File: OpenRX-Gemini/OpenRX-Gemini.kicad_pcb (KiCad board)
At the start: 6 copper layers, 54 x 14.2 mm, 194 parts, among them T1 0900PC16J0042001E, T4 0900PC16J0042001E, T5 0900PC16J0042001E, U1 ESP32-C3FH4, U1 OW7EL89CENUYO3YLC-32M, U15 RFX2401C, U16 SKY13414-485LF, U17 RFX2401C, U18 SKY13414-485LF, U2 LR1121IMLTRT, U2 TLV75533PDQNR, U3 ESP32-C3FH4, U3 SX1281IMLTRT, U3 TS2306A 240GF MSM 9_C2976675, U4 LR1121IMLTRT, U4 TS2306A 240GF MSM 9_C2976675, U5 OW7EL89CENUYO3YLC-32M, U6 TLV75533PDQNR, U7 RFX2401C, U8 SKY13414-485LF, U9 LR1121IMLTRT, X1 CJ17-400001010B20

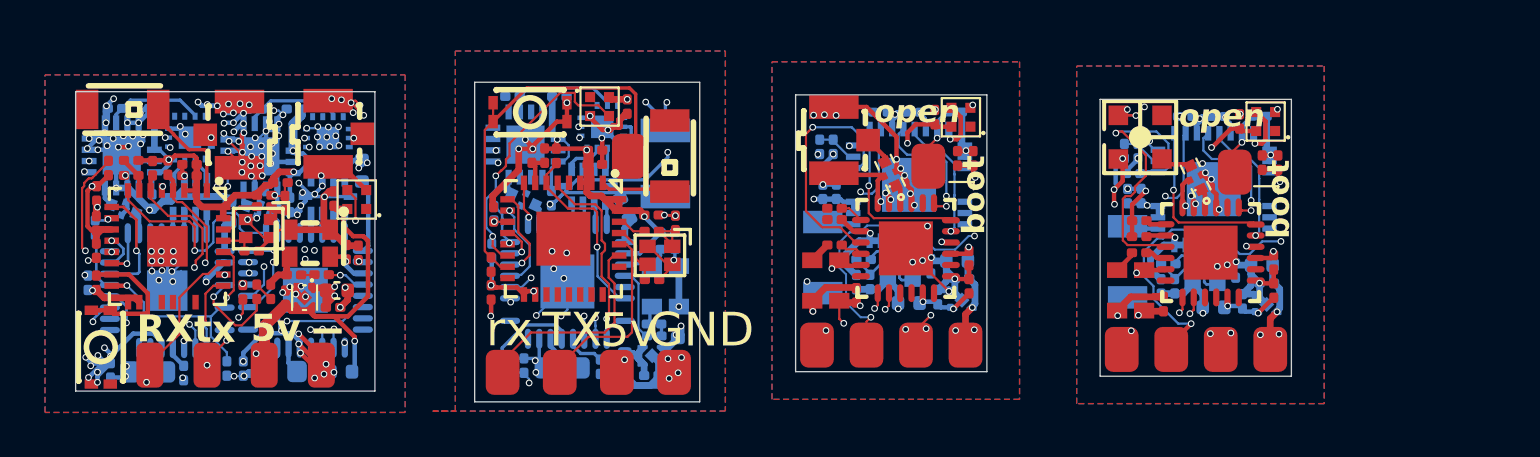
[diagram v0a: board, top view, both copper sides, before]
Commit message: switch to 0.2mm vias
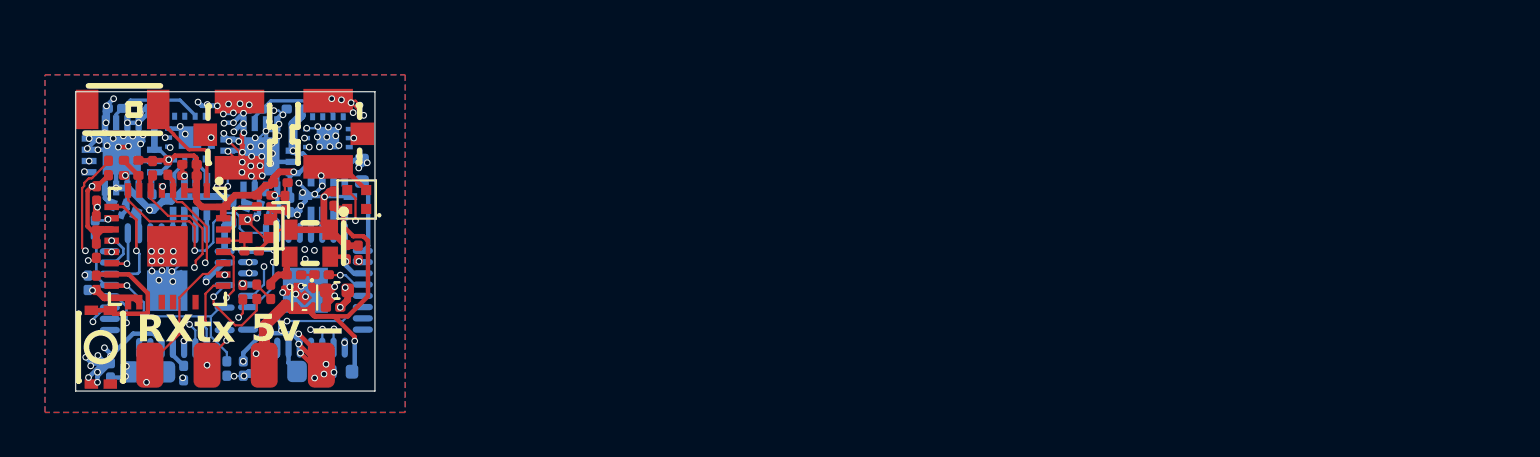
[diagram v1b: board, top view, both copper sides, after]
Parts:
- removed the AE1 at (87.8, 47.6)
- removed the AE1 at (108.1, 52.3)
- removed the AE1 at (94.6, 52.1)
- removed AE2: 47948-0001, OpenRX-Shared:ANT-SMD_47948-0001
- removed the C1 at (84.4, 47.4)
- removed the C1 at (96.7, 53.2)
- removed the C1 at (110.2, 53.4)
- removed the C10 at (100.7, 53.1)
- removed the C10 at (114.3, 53.3)
- removed the C11 at (100.5, 47.7)
- removed the C11 at (114.1, 47.9)
- removed the C11 at (88.1, 56.2)
- removed the C12 at (110.7, 45.9)
- removed the C12 at (85.8, 56.9)
- removed the C12 at (97.1, 45.7)
- removed the C13 at (96.0, 53.8)
- removed the C13 at (109.7, 54.2)
- removed the C13 at (87.1, 55.6)
- removed the C14 at (108.6, 51.2)
- removed the C14 at (95.1, 50.4)
- removed the C14 at (82.5, 49.5)
- removed the C15 at (99.7, 53.9)
- removed the C15 at (113.2, 54.1)
- removed the C15 at (82.9, 45.0)
- removed the C16 at (80.8, 45.0)
- removed the C16 at (111.9, 54.3)
- removed the C16 at (98.4, 54.1)
- removed the C17 at (114.6, 52.3)
- removed the C17 at (101.1, 52.1)
- removed the C18 at (85.9, 45.4)
- removed the C18 at (101.1, 53.4)
- removed the C18 at (114.6, 53.6)
- removed C19: 1uF, Capacitor_SMD:C_0201_0603Metric
- removed C19 (x2): 1nF, Capacitor_SMD:C_0201_0603Metric
- removed the C2 at (84.4, 48.0)
- removed the C2 at (94.4, 47.2)
- removed the C2 at (108.0, 47.4)
- removed the C20 at (108.6, 50.5)
- removed the C20 at (95.1, 49.9)
- removed the C20 at (85.8, 49.9)
- removed C21, C23, C5 (x3): 100nF, Capacitor_SMD:C_0201_0603Metric
- removed the C22 at (84.7, 57.0)
- removed the C24 at (81.3, 56.9)
- removed the C3 at (79.8, 53.7)
- removed the C3 at (99.4, 52.5)
- removed the C3 at (112.9, 52.7)
- removed the C4 at (109.6, 53.4)
- removed the C4 at (96.0, 53.2)
- removed the C4 at (80.7, 56.9)
- removed the C6 at (88.0, 50.6)
- removed the C6 at (108.1, 49.4)
- removed the C6 at (94.6, 49.2)
- removed the C7 at (113.1, 46.1)
- removed the C7 at (87.0, 53.1)
- removed the C7 at (99.5, 45.9)
- removed the C8 at (81.6, 47.6)
- removed the C8 at (100.5, 52.3)
- removed the C8 at (114.1, 52.5)
- removed the C9 at (101.2, 47.7)
- removed the C9 at (114.8, 47.9)
- removed the C9 at (86.9, 57.4)
- removed the D1 at (114.2, 46.1)
- removed the D1 at (100.7, 45.9)
- removed the D1 at (84.6, 45.4)
- removed FL1 (x3): 2450FM07D0034T, OpenRX-Shared:FILTER-SMD_4P-L1.0-W0.5-L
- removed JP1 (x2): U.FL-R-SMT-1(80), OpenRX-Shared:RF-SMD_FRF05002-JSS103M
- removed the L1 at (83.0, 57.0)
- removed the L1 at (109.9, 52.4)
- removed the L1 at (96.4, 52.2)
- removed the L2 at (87.0, 51.0)
- removed OSC1 (x2): OW7EL89CENUNFAYLC-52M, OpenRX-Shared:OSC-SMD_4P-L2.0-W1.6-BL_TXC_7Z
- removed the R1 at (82.2, 47.6)
- removed the R1 at (95.0, 47.2)
- removed the R1 at (108.6, 47.4)
- removed the R2 at (108.3, 48.4)
- removed the R2 at (94.8, 48.2)
- removed the R2 at (80.0, 50.1)
- removed the R3 at (79.8, 52.4)
- removed the R3 at (98.6, 45.7)
- removed the R3 at (112.1, 45.9)
- removed the R4 at (82.7, 47.6)
- removed the R4 at (100.4, 45.6)
- removed the R4 at (114.0, 45.8)
- removed the R5 at (79.8, 51.8)
- removed the R6 at (87.1, 55.1)
- removed T1: 0900PC16J0042001E, OpenRX-Shared:FILTER-SMD_10P-L2.0-W1.6-BL
- removed the TP1 at (107.8, 56.2)
- removed the TP1 at (80.3, 57.2)
- removed the TP1 at (94.3, 56.0)
- removed the TP2 at (82.9, 57.2)
- removed the TP2 at (96.5, 56.0)
- removed the TP2 at (110.0, 56.2)
- removed the TP3 at (100.9, 56.0)
- removed the TP3 at (85.4, 57.2)
- removed the TP3 at (114.4, 56.2)
- removed the TP4 at (98.7, 56.0)
- removed the TP4 at (88.0, 57.2)
- removed the TP4 at (112.2, 56.2)
- removed TP5: Boot, OpenRX-Shared:SolderPad_1.2x2.0mm
- removed TP5 (x2): GND, OpenRX-Shared:SolderPad_1.2x2.0mm
- removed the U1 at (83.0, 51.3)
- removed the U1 at (111.9, 49.1)
- removed the U1 at (98.4, 48.9)
- removed the U2 at (114.3, 54.2)
- removed the U2 at (87.0, 56.5)
- removed the U2 at (100.7, 54.0)
- removed the U3 at (111.8, 51.9)
- removed the U3 at (98.2, 51.7)
- removed the U3 at (81.5, 45.7)
- removed the U4 at (83.2, 53.2)
- removed U5: OW7EL89CENUYO3YLC-32M, OpenRX-Shared:OSC-SMD_4P-L2.0-W1.6-BL_TXC_7Z
- removed U7: RFX2401C, OpenRX-Shared:QFN-16_L3.0-W3.0-P0.50-BL-EP1.7
- removed U8: SKY13414-485LF, OpenRX-Shared:QFN-14_L2.0-W2.0-P0.45-BL-EP
- removed the X1 at (87.3, 52.0)
- removed the X1 at (98.0, 52.7)
- removed the X1 at (111.5, 52.9)
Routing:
- net GND: track 296.8 -> 155.9 mm, vias 220 -> 136
- net +3V3: track 121.9 -> 50.4 mm, vias 42 -> 14
- net +5V: track 66.8 -> 17.7 mm, vias 12 -> 2
- net Net-(U1-U0RXD): track 32.2 -> 0.00 mm, vias 4 -> 0
- net Net-(U1-U0TXD): track 27.9 -> 0.00 mm, vias 2 -> 0
- net /ESP32-C3 + LR1121 Mono/BUTTON: track 18.2 -> 0.00 mm
- net /ESP32-C3 + SX1281 Core/RST: track 13.2 -> 0.00 mm, vias 1 -> 0
- net /ESP32-C3 + LR1121 Mono/LED: track 12.0 -> 0.00 mm, vias 2 -> 0
- net /ESP32-C3 + SX1281 Core (UFL)/RST: track 11.8 -> 0.00 mm, vias 1 -> 0
- net /ESP32-C3 + LR1121 Mono/DIO8-1: track 10.2 -> 0.00 mm, vias 2 -> 0
- net /ESP32-C3 + SX1281 Core/DIO1: track 10.0 -> 0.00 mm, vias 2 -> 0
- net /ESP32-C3 + SX1281 Core (UFL)/DIO1: track 10.0 -> 0.00 mm, vias 2 -> 0
- net /ESP32-C3 + SX1281 Core/BUSY: track 9.55 -> 0.00 mm, vias 2 -> 0
- net /ESP32-C3 + LR1121 Mono/DIO7-1: track 9.16 -> 0.00 mm, vias 2 -> 0
- net /ESP32-C3 + SX1281 Core (UFL)/BUSY: track 8.60 -> 0.00 mm, vias 2 -> 0
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- removed copper zone on In3.Cu, net +3V3
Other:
- board size 54 x 14.2 mm -> 13.3 x 13.3 mm
- board text removed: "GND"
- board text removed: "TX"
- board text removed: "boot"
- board text removed: "open"
- board text removed: "rx"

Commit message: Update OpenRX-Gemini.kicad_pcb
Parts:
- added AE1: 2450AT18A100E, OpenRX-Shared:ANT-SMD_L3.2-W1.6, F.Cu at (94.9, 47.0)
- added AE1: 2450AT18A100E, OpenRX-Shared:ANT-SMD_L3.2-W1.6, B.Cu at (115.6, 51.6)
- added AE1: 2450AT18A100E, OpenRX-Shared:ANT-SMD_L3.2-W1.6, B.Cu at (102.0, 51.6)
- added AE2: 47948-0001, OpenRX-Shared:ANT-SMD_47948-0001, F.Cu at (116.2, 46.1)
- added C1: 100nF, Capacitor_SMD:C_0201_0603Metric, F.Cu at (91.5, 46.7)
- added C1: 18pF, Capacitor_SMD:C_0201_0603Metric, B.Cu at (104.1, 52.7)
- added C1: 18pF, Capacitor_SMD:C_0201_0603Metric, B.Cu at (117.7, 52.7)
- added C10: 1uF, Capacitor_SMD:C_0201_0603Metric, B.Cu at (108.2, 52.6)
- added C10: 1uF, Capacitor_SMD:C_0201_0603Metric, B.Cu at (121.8, 52.6)
- added C11: 100nF, Capacitor_SMD:C_0201_0603Metric, F.Cu at (108.0, 47.2)
- added C11: 100nF, Capacitor_SMD:C_0201_0603Metric, F.Cu at (121.6, 47.2)
- added C11: 10uF, Capacitor_SMD:C_0402_1005Metric, B.Cu at (95.2, 55.5)
- added C12: 100nF, Capacitor_SMD:C_0201_0603Metric, B.Cu at (104.6, 45.1)
- added C12: 100nF, Capacitor_SMD:C_0201_0603Metric, B.Cu at (118.2, 45.1)
- added C12: 10uF, Capacitor_SMD:C_0402_1005Metric, B.Cu at (92.9, 56.2)
- added C13: 100nF, Capacitor_SMD:C_0201_0603Metric, F.Cu at (103.5, 53.3)
- added C13: 100nF, Capacitor_SMD:C_0201_0603Metric, F.Cu at (117.2, 53.5)
- added C13: 10pF, Capacitor_SMD:C_0201_0603Metric, B.Cu at (94.2, 55.0)
- added C14: 100nF, Capacitor_SMD:C_0201_0603Metric, F.Cu at (116.1, 50.5)
- added C14: 100nF, Capacitor_SMD:C_0201_0603Metric, F.Cu at (102.5, 49.9)
- added C14: 1uF, Capacitor_SMD:C_0201_0603Metric, B.Cu at (89.6, 48.8)
- added C15: 220pF, Capacitor_SMD:C_0201_0603Metric, B.Cu at (90.0, 44.3)
- added C15: 1uF, Capacitor_SMD:C_0201_0603Metric, B.Cu at (120.7, 53.4)
- added C15: 1uF, Capacitor_SMD:C_0201_0603Metric, B.Cu at (107.1, 53.4)
- added C16: 0.3pF, Capacitor_SMD:C_0201_0603Metric, B.Cu at (87.9, 44.3)
- added C16: 10uF, Capacitor_SMD:C_0402_1005Metric, B.Cu at (105.8, 53.6)
- added C16: 10uF, Capacitor_SMD:C_0402_1005Metric, B.Cu at (119.4, 53.6)
- added C17: 100nF, Capacitor_SMD:C_0201_0603Metric, F.Cu at (122.1, 51.6)
- added C17: 100nF, Capacitor_SMD:C_0201_0603Metric, F.Cu at (108.5, 51.6)
- added C18: 100nF, Capacitor_SMD:C_0201_0603Metric, F.Cu at (122.1, 52.9)
- added C18: 100nF, Capacitor_SMD:C_0201_0603Metric, F.Cu at (93.0, 44.8)
- added C18: 100nF, Capacitor_SMD:C_0201_0603Metric, F.Cu at (108.5, 52.9)
- added C19: 1uF, Capacitor_SMD:C_0201_0603Metric, F.Cu at (94.1, 49.6)
- added C19: 1nF, Capacitor_SMD:C_0201_0603Metric, F.Cu at (102.5, 51.0)
- added C19: 1nF, Capacitor_SMD:C_0201_0603Metric, F.Cu at (116.1, 51.2)
- added C2: 100nF, Capacitor_SMD:C_0201_0603Metric, F.Cu at (91.5, 47.3)
- added C2: 1uF, Capacitor_SMD:C_0201_0603Metric, B.Cu at (115.5, 46.7)
- added C2: 1uF, Capacitor_SMD:C_0201_0603Metric, B.Cu at (101.9, 46.7)
- added C20: 470nF, Capacitor_SMD:C_0201_0603Metric, F.Cu at (116.1, 49.8)
- added C20: 470nF, Capacitor_SMD:C_0201_0603Metric, F.Cu at (102.5, 49.4)
- added C20: 4.7uF, Capacitor_SMD:C_0402_1005Metric, B.Cu at (92.9, 49.3)
- added C21: 100nF, Capacitor_SMD:C_0201_0603Metric, B.Cu at (94.8, 50.4)
- added C22: 100nF, Capacitor_SMD:C_0201_0603Metric, B.Cu at (91.8, 56.3)
- added C23: 100nF, Capacitor_SMD:C_0201_0603Metric, B.Cu at (94.8, 51.1)
- added C24: 100nF, Capacitor_SMD:C_0201_0603Metric, B.Cu at (88.4, 56.3)
- added C3: 100nF, Capacitor_SMD:C_0201_0603Metric, F.Cu at (86.9, 53.0)
- added C3: 18pF, Capacitor_SMD:C_0201_0603Metric, B.Cu at (106.8, 52.0)
- added C3: 18pF, Capacitor_SMD:C_0201_0603Metric, B.Cu at (120.4, 52.0)
- added C4: 100nF, Capacitor_SMD:C_0201_0603Metric, B.Cu at (87.8, 56.3)
- added C4: 1uF, Capacitor_SMD:C_0201_0603Metric, B.Cu at (117.1, 52.7)
- added C4: 1uF, Capacitor_SMD:C_0201_0603Metric, B.Cu at (103.5, 52.7)
- added C5: 100nF, Capacitor_SMD:C_0201_0603Metric, F.Cu at (87.0, 49.6)
- added C5: 100nF, Capacitor_SMD:C_0201_0603Metric, B.Cu at (116.2, 48.7)
- added C5: 100nF, Capacitor_SMD:C_0201_0603Metric, B.Cu at (102.6, 48.7)
- added C6: 18pF, Capacitor_SMD:C_0201_0603Metric, F.Cu at (95.1, 49.9)
- added C6: 100nF, Capacitor_SMD:C_0201_0603Metric, B.Cu at (115.6, 48.7)
- added C6: 100nF, Capacitor_SMD:C_0201_0603Metric, B.Cu at (102.0, 48.7)
- added C7: 100nF, Capacitor_SMD:C_0201_0603Metric, F.Cu at (107.0, 45.4)
- added C7: 100nF, Capacitor_SMD:C_0201_0603Metric, F.Cu at (120.6, 45.4)
- added C7: 18pF, Capacitor_SMD:C_0201_0603Metric, F.Cu at (94.1, 52.5)
- added C8: 1uF, Capacitor_SMD:C_0201_0603Metric, F.Cu at (88.7, 47.0)
- added C8: 10uF, Capacitor_SMD:C_0402_1005Metric, B.Cu at (121.6, 51.8)
- added C8: 10uF, Capacitor_SMD:C_0402_1005Metric, B.Cu at (108.0, 51.8)
- added C9: 100nF, Capacitor_SMD:C_0201_0603Metric, F.Cu at (108.7, 47.2)
- added C9: 100nF, Capacitor_SMD:C_0201_0603Metric, F.Cu at (122.3, 47.2)
- added C9: 1uF, Capacitor_SMD:C_0201_0603Metric, B.Cu at (94.0, 56.7)
- added D1: XL-1010RGBC-WS2812B, OpenRX-Shared:LED-SMD_4P-L1.0-W1.0-TL_XL-1010RGBC-WS2812B, F.Cu at (108.2, 45.4)
- added D1: XL-1010RGBC-WS2812B, OpenRX-Shared:LED-SMD_4P-L1.0-W1.0-TL_XL-1010RGBC-WS2812B, F.Cu at (91.8, 44.8)
- added D1: XL-1010RGBC-WS2812B, OpenRX-Shared:LED-SMD_4P-L1.0-W1.0-TL_XL-1010RGBC-WS2812B, F.Cu at (121.7, 45.4)
- added FL1: 2450FM07D0034T, OpenRX-Shared:FILTER-SMD_4P-L1.0-W0.5-L, F.Cu at (118.6, 47.9)
- added FL1: 2450FM07D0034T, OpenRX-Shared:FILTER-SMD_4P-L1.0-W0.5-L, F.Cu at (105.0, 47.9)
- added FL1: 2450FM07D0034T, OpenRX-Shared:FILTER-SMD_4P-L1.0-W0.5-L, B.Cu at (88.4, 48.9)
- added JP1: U.FL-R-SMT-1(80), OpenRX-Shared:RF-SMD_FRF05002-JSS103M, F.Cu at (103.3, 46.4)
- added JP1: U.FL-R-SMT-1(80), OpenRX-Shared:RF-SMD_FRF05002-JSS103M, B.Cu at (93.9, 47.3)
- added L1: 10uH, Inductor_SMD:L_0603_1608Metric, B.Cu at (90.1, 56.4)
- added L1: 24nH, Inductor_SMD:L_0201_0603Metric, B.Cu at (117.4, 51.7)
- added L1: 24nH, Inductor_SMD:L_0201_0603Metric, B.Cu at (103.8, 51.7)
- added L2: 24nH, Inductor_SMD:L_0201_0603Metric, F.Cu at (94.1, 50.3)
- added OSC1: OW7EL89CENUNFAYLC-52M, OpenRX-Shared:OSC-SMD_4P-L2.0-W1.6-BL_TXC_7Z, F.Cu at (102.2, 52.6)
- added OSC1: OW7EL89CENUNFAYLC-52M, OpenRX-Shared:OSC-SMD_4P-L2.0-W1.6-BL_TXC_7Z, F.Cu at (115.7, 52.9)
- added R1: 10k, Resistor_SMD:R_0201_0603Metric, F.Cu at (89.3, 47.0)
- added R1: 10k, Resistor_SMD:R_0201_0603Metric, B.Cu at (102.5, 46.7)
- added R1: 10k, Resistor_SMD:R_0201_0603Metric, B.Cu at (116.0, 46.7)
- added R2: 10k, Resistor_SMD:R_0201_0603Metric, B.Cu at (115.8, 47.7)
- added R2: 10k, Resistor_SMD:R_0201_0603Metric, B.Cu at (87.1, 49.5)
- added R2: 10k, Resistor_SMD:R_0201_0603Metric, B.Cu at (102.3, 47.7)
- added R3: 10k, Resistor_SMD:R_0201_0603Metric, F.Cu at (86.9, 51.8)
- added R3: 10k, Resistor_SMD:R_0201_0603Metric, B.Cu at (119.6, 45.1)
- added R3: 10k, Resistor_SMD:R_0201_0603Metric, B.Cu at (106.0, 45.1)
- added R4: 10k, Resistor_SMD:R_0201_0603Metric, F.Cu at (89.8, 47.0)
- added R4: 10k, Resistor_SMD:R_0201_0603Metric, B.Cu at (107.9, 45.1)
- added R4: 10k, Resistor_SMD:R_0201_0603Metric, B.Cu at (121.5, 45.1)
- added R5: 10k, Resistor_SMD:R_0201_0603Metric, B.Cu at (87.0, 51.2)
- added R6: 220R, Resistor_SMD:R_0201_0603Metric, B.Cu at (94.2, 54.4)
- added T1: 0900PC16J0042001E, OpenRX-Shared:FILTER-SMD_10P-L2.0-W1.6-BL, B.Cu at (91.3, 48.3)
- added TP1: RX, OpenRX-Shared:SolderPad_1.2x2.0mm, F.Cu at (115.3, 55.5)
- added TP1: RX, OpenRX-Shared:SolderPad_1.2x2.0mm, F.Cu at (101.8, 55.5)
- added TP1: RX, OpenRX-Shared:SolderPad_1.2x2.0mm, F.Cu at (87.4, 56.6)
- added TP2: TX, OpenRX-Shared:SolderPad_1.2x2.0mm, F.Cu at (104.0, 55.5)
- added TP2: TX, OpenRX-Shared:SolderPad_1.2x2.0mm, F.Cu at (117.5, 55.5)
- added TP2: TX, OpenRX-Shared:SolderPad_1.2x2.0mm, F.Cu at (90.0, 56.6)
- added TP3: 5V, OpenRX-Shared:SolderPad_1.2x2.0mm, F.Cu at (108.4, 55.5)
- added TP3: 5V, OpenRX-Shared:SolderPad_1.2x2.0mm, F.Cu at (92.5, 56.6)
- added TP3: 5V, OpenRX-Shared:SolderPad_1.2x2.0mm, F.Cu at (121.9, 55.5)
- added TP4: GND, OpenRX-Shared:SolderPad_1.2x2.0mm, F.Cu at (119.7, 55.5)
- added TP4: GND, OpenRX-Shared:SolderPad_1.2x2.0mm, F.Cu at (106.2, 55.5)
- added TP4: GND, OpenRX-Shared:SolderPad_1.2x2.0mm, F.Cu at (95.1, 56.6)
- added TP5: Boot, OpenRX-Shared:SolderPad_1.2x2.0mm, F.Cu at (93.0, 47.0)
- added TP5: GND, OpenRX-Shared:SolderPad_1.2x2.0mm, F.Cu at (106.7, 47.5)
- added TP5: GND, OpenRX-Shared:SolderPad_1.2x2.0mm, F.Cu at (120.4, 47.6)
- added U1: ESP32-C3FH4, OpenRX-Shared:QFN-32_L5.0-W5.0-P0.50-TL-EP3.7, F.Cu at (90.1, 50.6)
- added U1: ESP32-C3FH4, OpenRX-Shared:QFN-32_L5.0-W5.0-P0.50-TL-EP3.7, B.Cu at (119.4, 48.4)
- added U1: ESP32-C3FH4, OpenRX-Shared:QFN-32_L5.0-W5.0-P0.50-TL-EP3.7, B.Cu at (105.9, 48.4)
- added U2: TLV75533PDQNR, OpenRX-Shared:X2SON-4_L1.0-W1.0-P0.65-TL-EP, B.Cu at (94.1, 55.8)
- added U2: TLV75533PDQNR, OpenRX-Shared:X2SON-4_L1.0-W1.0-P0.65-TL-EP, B.Cu at (121.8, 53.5)
- added U2: TLV75533PDQNR, OpenRX-Shared:X2SON-4_L1.0-W1.0-P0.65-TL-EP, B.Cu at (108.2, 53.5)
- added U3: SX1281IMLTRT, OpenRX-Shared:QFN-24_L4.0-W4.0-P0.50-TL-EP2.6, F.Cu at (105.7, 51.2)
- added U3: SX1281IMLTRT, OpenRX-Shared:QFN-24_L4.0-W4.0-P0.50-TL-EP2.6, F.Cu at (119.3, 51.2)
- added U3: TS2306A 240GF MSM 9_C2976675, OpenRX-Shared:SW-SMD_4P-L3.0-W2.0-P0.85-LS3.5, F.Cu at (88.7, 45.0)
- added U4: LR1121IMLTRT, OpenRX-Shared:QFN-32_L5.0-W5.0-P0.50-BL-EP3.7, B.Cu at (90.3, 52.5)
- added U5: OW7EL89CENUYO3YLC-32M, OpenRX-Shared:OSC-SMD_4P-L2.0-W1.6-BL_TXC_7Z, B.Cu at (94.7, 52.8)
- added U7: RFX2401C, OpenRX-Shared:QFN-16_L3.0-W3.0-P0.50-BL-EP1.7, B.Cu at (88.5, 46.5)
- added U8: SKY13414-485LF, OpenRX-Shared:QFN-14_L2.0-W2.0-P0.45-BL-EP, B.Cu at (91.9, 45.7)
- added X1: CJ17-400001010B20, OpenRX-Shared:CRYSTAL-SMD_4P-L1.6-W1.2-BL, F.Cu at (94.4, 51.4)
- added X1: CJ17-400001010B20, OpenRX-Shared:CRYSTAL-SMD_4P-L1.6-W1.2-BL, B.Cu at (119.0, 52.2)
- added X1: CJ17-400001010B20, OpenRX-Shared:CRYSTAL-SMD_4P-L1.6-W1.2-BL, B.Cu at (105.5, 52.2)
- moved C1 6.96 mm to (77.5, 48.6)
- moved C12 6.96 mm to (79.7, 48.4)
- moved C13 6.96 mm to (69.8, 56.0)
- moved C14 6.96 mm to (80.0, 56.0)
- moved C2 6.96 mm to (70.7, 47.3)
- moved C20 6.96 mm to (79.7, 53.2)
- moved C22 6.96 mm to (79.8, 52.4)
- moved C26 6.96 mm to (78.8, 56.0)
- moved C28 6.96 mm to (80.9, 47.1)
- moved C3 6.96 mm to (77.3, 47.6)
- moved C42 6.96 mm to (70.0, 44.4)
- moved C45 6.96 mm to (76.2, 44.4)
- moved C46 6.96 mm to (77.7, 48.6)
- moved C6 6.96 mm to (76.6, 48.2)
- moved C7 6.96 mm to (73.0, 56.1)
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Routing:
- net GND: track 155.9 -> 298.1 mm, vias 136 -> 220
- net +3V3: track 50.4 -> 121.9 mm, vias 14 -> 42
- net +5V: track 17.7 -> 66.8 mm, vias 2 -> 12
- net Net-(U1-U0RXD): track 0.00 -> 32.2 mm, vias 0 -> 4
- net Net-(U1-U0TXD): track 0.00 -> 29.5 mm, vias 0 -> 2
- net /ESP32-C3 + LR1121 Mono/BUTTON: track 0.00 -> 18.2 mm
- net /ESP32-C3 + SX1281 Core/RST: track 0.00 -> 13.2 mm, vias 0 -> 1
- net /ESP32-C3 + LR1121 Mono/LED: track 0.00 -> 12.0 mm, vias 0 -> 2
- net /ESP32-C3 + SX1281 Core (UFL)/RST: track 0.00 -> 11.8 mm, vias 0 -> 1
- net /ESP32-C3 + SX1281 Core/DIO1: track 0.00 -> 10.0 mm, vias 0 -> 2
- net /ESP32-C3 + SX1281 Core (UFL)/DIO1: track 0.00 -> 10.0 mm, vias 0 -> 2
- net /ESP32-C3 + LR1121 Mono/DIO8-1: track 0.00 -> 9.95 mm, vias 0 -> 2
- net /ESP32-C3 + SX1281 Core/BUSY: track 0.00 -> 9.55 mm, vias 0 -> 2
- net /ESP32-C3 + LR1121 Mono/DIO7-1: track 0.00 -> 9.25 mm, vias 0 -> 2
- net /ESP32-C3 + SX1281 Core (UFL)/BUSY: track 0.00 -> 8.60 mm, vias 0 -> 2
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- added copper zone on In3.Cu, net +3V3
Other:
- board size 13.3 x 13.3 mm -> 57.6 x 16 mm
- board text added: "GND"
- board text added: "TX"
- board text added: "boot"
- board text added: "open"
- board text added: "rx"
